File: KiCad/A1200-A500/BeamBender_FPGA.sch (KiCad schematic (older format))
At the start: 27 parts, among them J6 Conn_02x06_Odd_Even, U2 GW1NR-UV9LQ144P, U5 AK5720VT, X3 5.0x3.2mm

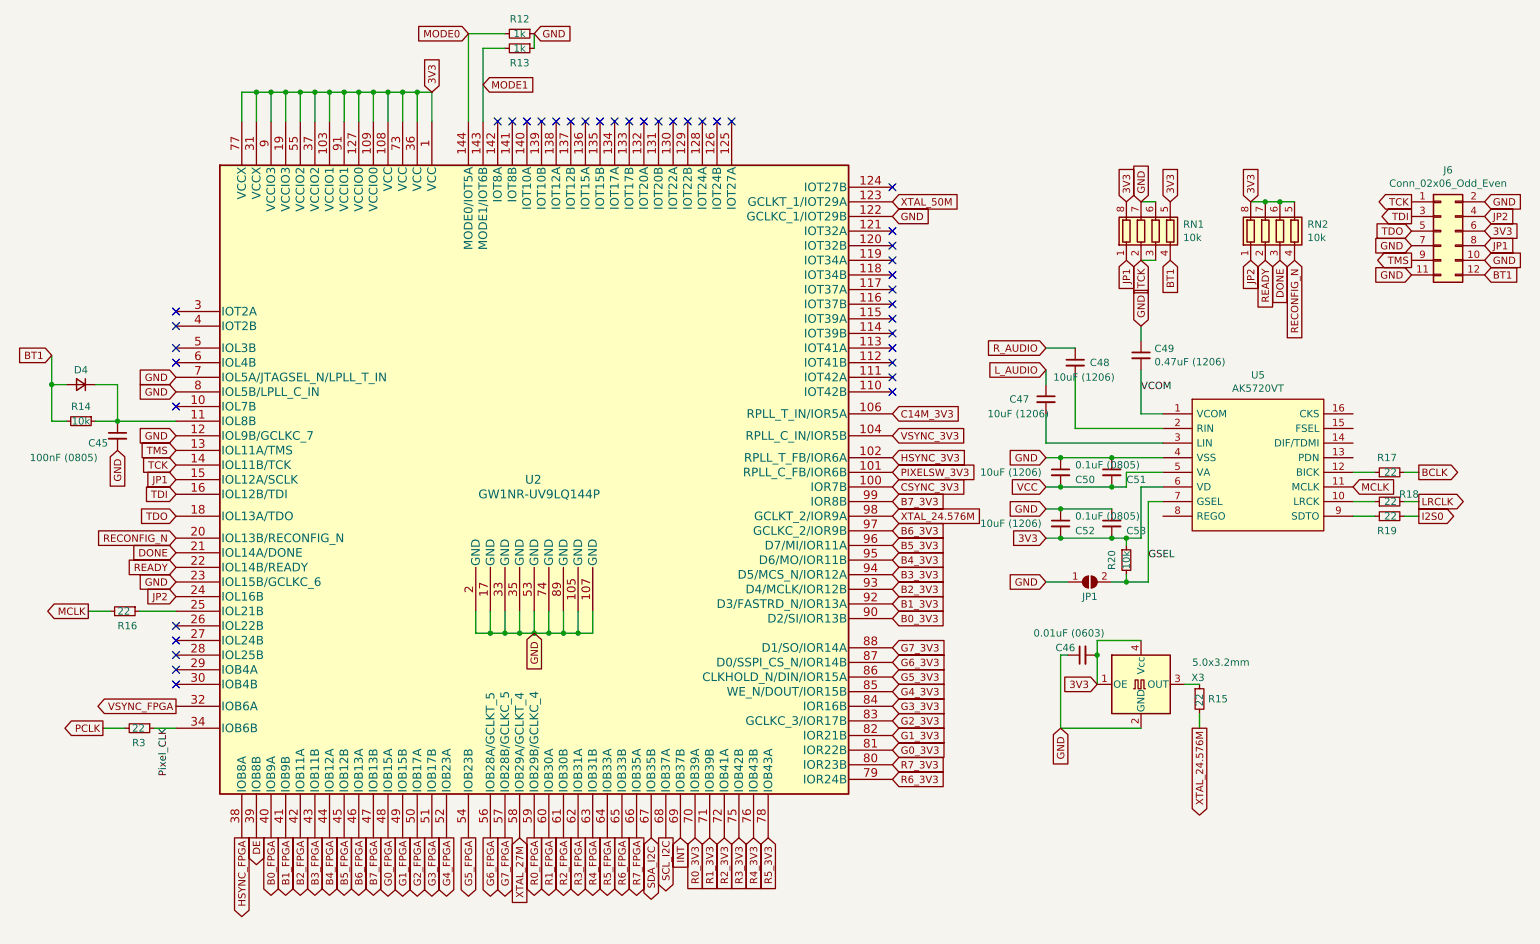
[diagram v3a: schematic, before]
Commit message: Finished routing the ak5720vt-chip, changed to a potential-divider for controlling GSEL-pin, PDN_RESET,FSEL and DIF-signals routed to spare pins in the FPGA
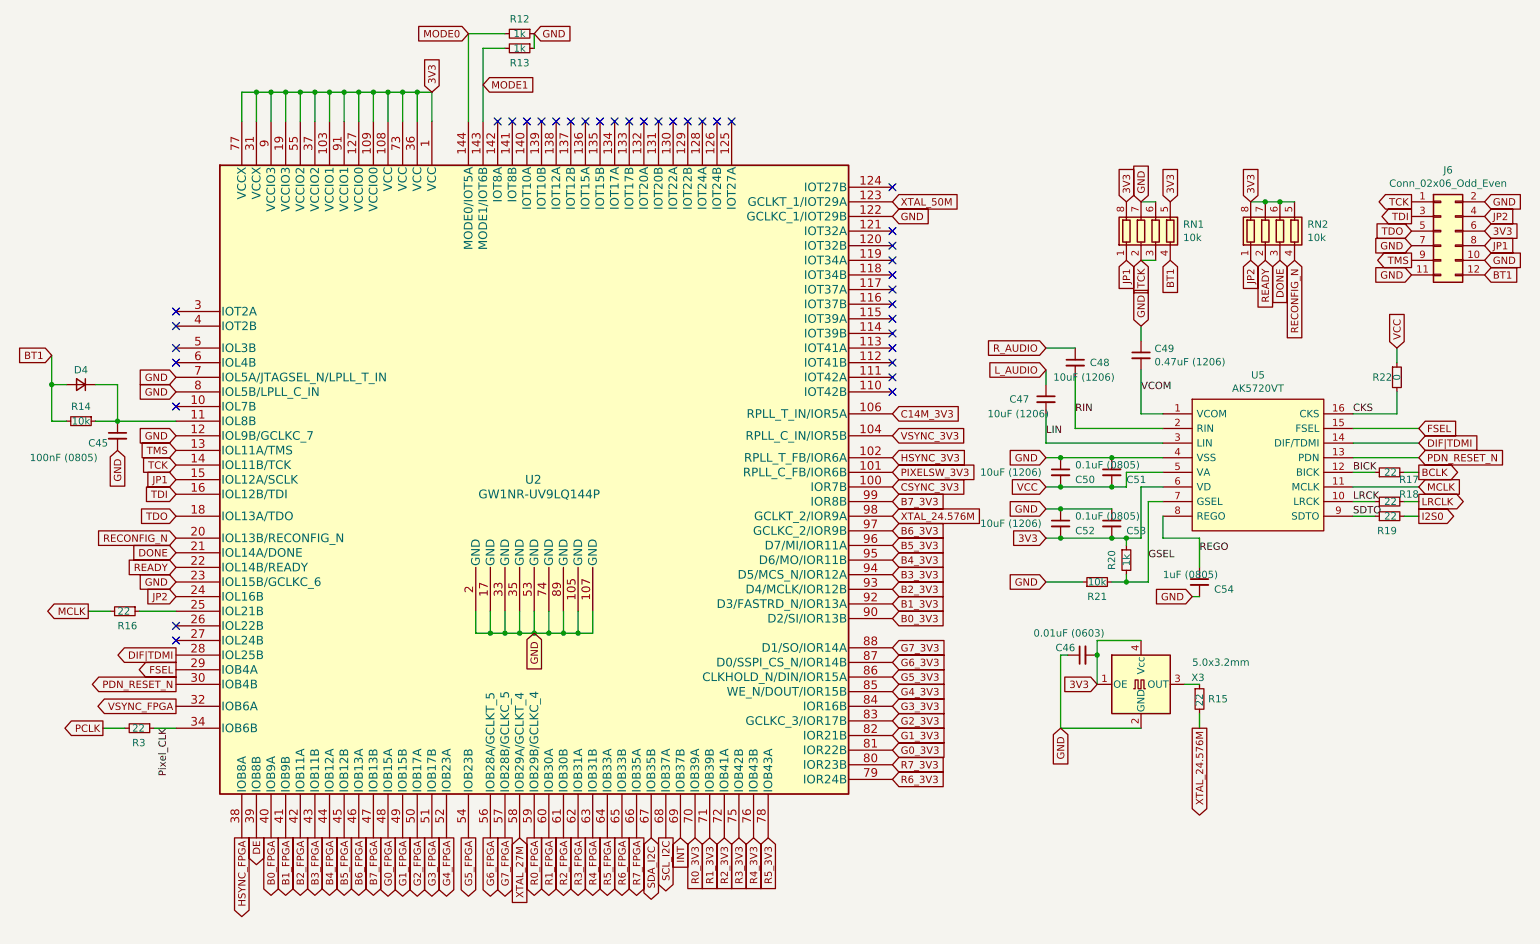
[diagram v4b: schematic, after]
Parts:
- removed JP1: SolderJumper_2_Open, Jumper:SolderJumper-2_P1.3mm_Open_Pad1.0x1.5mm, symbol Jumper:SolderJumper_2_Open
- added C54: 1uF (0805), Capacitor_SMD:C_0805_2012Metric_Pad1.18x1.45mm_HandSolder, symbol Device:C_Small
- added R21: 10k, Resistor_SMD:R_0805_2012Metric_Pad1.20x1.40mm_HandSolder, symbol Device:R_Small
- added R22: 0, Resistor_SMD:R_0805_2012Metric_Pad1.20x1.40mm_HandSolder, symbol Device:R_Small
- R20: value 10k -> 1k
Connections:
- net GND: now also C54.2, R21.1
- net GSEL: now also R21.2
- net VCC: now also R22.1
- net DIF|TDMI: now reaches U2.28 (IOL25B)
- net DIF|TDMI: now also U5.14 (DIF/TDMI)
- net FSEL: now reaches U2.29 (IOB4A)
- net FSEL: now also U5.15 (FSEL)
- net PDN_RESET_N: now reaches U2.30 (IOB4B)
- net PDN_RESET_N: now also U5.13 (PDN)
- net LRCK: now reaches R18.1, U5.10 (LRCK)
- net BICK: now reaches R17.1, U5.12 (BICK)
- net CKS: now reaches U5.16 (CKS)
- net CKS: now also R22.2
- net RIN: now reaches C48.2, U5.2 (RIN)
- net LIN: now reaches C47.2, U5.3 (LIN)
- net REGO: now reaches U5.8 (REGO)
- net REGO: now also C54.1
- net SDTO: now reaches R19.1, U5.9 (SDTO)
- no-connect marks 40 -> 37
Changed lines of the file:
@@
 NoConn ~ 1600 4700
 NoConn ~ 1600 4800
-NoConn ~ 1600 4900
-NoConn ~ 1600 5000
-NoConn ~ 1600 5100
 NoConn ~ 6500 1700
 NoConn ~ 6500 2000
@@
 Text GLabel 10100 3950 2    50   Output ~ 0
 I2S0
-Text GLabel 9650 3750 2    50   Input ~ 0
+Text GLabel 10100 3750 2    50   Input ~ 0
 MCLK
 Text GLabel 10100 3850 2    50   Output ~ 0
@@
 U 1 1 666AAB38
 P 9900 3650
-F 0 "R17" V 10000 3600 50  0000 L CNN
+F 0 "R17" V 9850 3450 50  0000 L CNN
 F 1 "22" V 9900 3600 50  0000 L CNN
 F 2 "Resistor_SMD:R_0603_1608Metric_Pad0.98x0.95mm_HandSolder" H 9900 3650 50  0001 C CNN
@@
 	8350 3850 8250 3850
 $Comp
-L Jumper:SolderJumper_2_Open JP1
-U 1 1 668D7347
-P 7850 4400
-F 0 "JP1" H 7850 4300 50  0000 C CNN
-F 1 "SolderJumper_2_Open" H 7850 4514 50  0001 C CNN
-F 2 "Jumper:SolderJumper-2_P1.3mm_Open_Pad1.0x1.5mm" H 7850 4400 50  0001 C CNN
-F 3 "~" H 7850 4400 50  0001 C CNN
-	1    7850 4400
-	1    0    0    -1
-$EndComp
-$Comp
 L Device:R_Small R20
 U 1 1 668DB86F
 P 8100 4250
 F 0 "R20" V 8000 4250 50  0000 C CNN
-F 1 "10k" V 8100 4250 50  0000 C CNN
+F 1 "1k" V 8100 4250 50  0000 C CNN
 F 2 "Resistor_SMD:R_0805_2012Metric_Pad1.20x1.40mm_HandSolder" H 8100 4250 50  0001 C CNN
 F 3 "~" H 8100 4250 50  0001 C CNN
@@
 GND
 Wire Wire Line
-	7550 4400 7700 4400
-Wire Wire Line
 	8100 4100 8100 4150
 Connection ~ 8100 4100
@@
 Text Label 8250 4250 0    50   ~ 0
 GSEL
+$Comp
+L Device:C_Small C?
+U 1 1 66921A02
+P 8600 4400
+AR Path="/66921A02" Ref="C?"  Part="1"
+AR Path="/6541C824/66921A02" Ref="C54"  Part="1"
+F 0 "C54" H 8700 4350 50  0000 L CNN
+F 1 "1uF (0805)" H 8350 4450 50  0000 L CNN
+F 2 "Capacitor_SMD:C_0805_2012Metric_Pad1.18x1.45mm_HandSolder" H 8600 4400 50  0001 C CNN
+F 3 "~" H 8600 4400 50  0001 C CNN
+	1    8600 4400
+	1    0    0    -1
+$EndComp
+Text GLabel 8550 4500 0    50   Input ~ 0
+GND
+Wire Wire Line
+	8550 4500 8600 4500
+Wire Wire Line
+	8350 3950 8350 4100
+Wire Wire Line
+	8350 4100 8600 4100
+Wire Wire Line
+	8600 4100 8600 4300
+Text Label 8600 4200 0    50   ~ 0
+REGO
+Text Label 7750 3250 0    50   ~ 0
+RIN
+Text Label 7550 3400 0    50   ~ 0
+LIN
+Text Label 9650 3650 0    50   ~ 0
+BICK
+Text Label 9650 3850 0    50   ~ 0
+LRCK
+Text Label 9650 3950 0    50   ~ 0
+SDTO
+Text Label 9650 3250 0    50   ~ 0
+CKS
+$Comp
+L Device:R_Small R22
+U 1 1 66968A2E
+P 9950 3000
+F 0 "R22" H 9850 3000 50  0000 C CNN
+F 1 "0" V 9950 3000 50  0000 C CNN
+F 2 "Resistor_SMD:R_0805_2012Metric_Pad1.20x1.40mm_HandSolder" H 9950 3000 50  0001 C CNN
+F 3 "~" H 9950 3000 50  0001 C CNN
+	1    9950 3000
+	1    0    0    -1
+$EndComp
+Wire Wire Line
+	9650 3250 9950 3250
+Wire Wire Line
+	9950 3250 9950 3100
+Text GLabel 9950 2800 1    50   Input ~ 0
+VCC
+Wire Wire Line
+	9950 2900 9950 2800
+Text GLabel 10100 3450 2    50   Input ~ 0
+DIF|TDMI
+Wire Wire Line
+	9650 3450 10100 3450
+Text GLabel 10100 3550 2    50   Input ~ 0
+PDN_RESET_N
+Wire Wire Line
+	10100 3550 9650 3550
+Wire Wire Line
+	9650 3750 10100 3750
+Text GLabel 1600 5100 0    50   Output ~ 0
+PDN_RESET_N
+Text GLabel 1600 4900 0    50   Output ~ 0
+DIF|TDMI
+Text GLabel 10100 3350 2    50   Input ~ 0
+FSEL
+Wire Wire Line
+	9650 3350 10100 3350
+Text GLabel 1600 5000 0    50   Output ~ 0
+FSEL
+$Comp
+L Device:R_Small R21
+U 1 1 66A36561
+P 7900 4400
+F 0 "R21" V 7800 4400 50  0000 C CNN
+F 1 "10k" V 7900 4400 50  0000 C CNN
+F 2 "Resistor_SMD:R_0805_2012Metric_Pad1.20x1.40mm_HandSolder" H 7900 4400 50  0001 C CNN
+F 3 "~" H 7900 4400 50  0001 C CNN
+	1    7900 4400
+	0    -1   -1   0
+$EndComp
+Wire Wire Line
+	7550 4400 7800 4400
 $EndSCHEMATC

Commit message: Fixed assignment/enumeration of all capacitors from C1 to C54
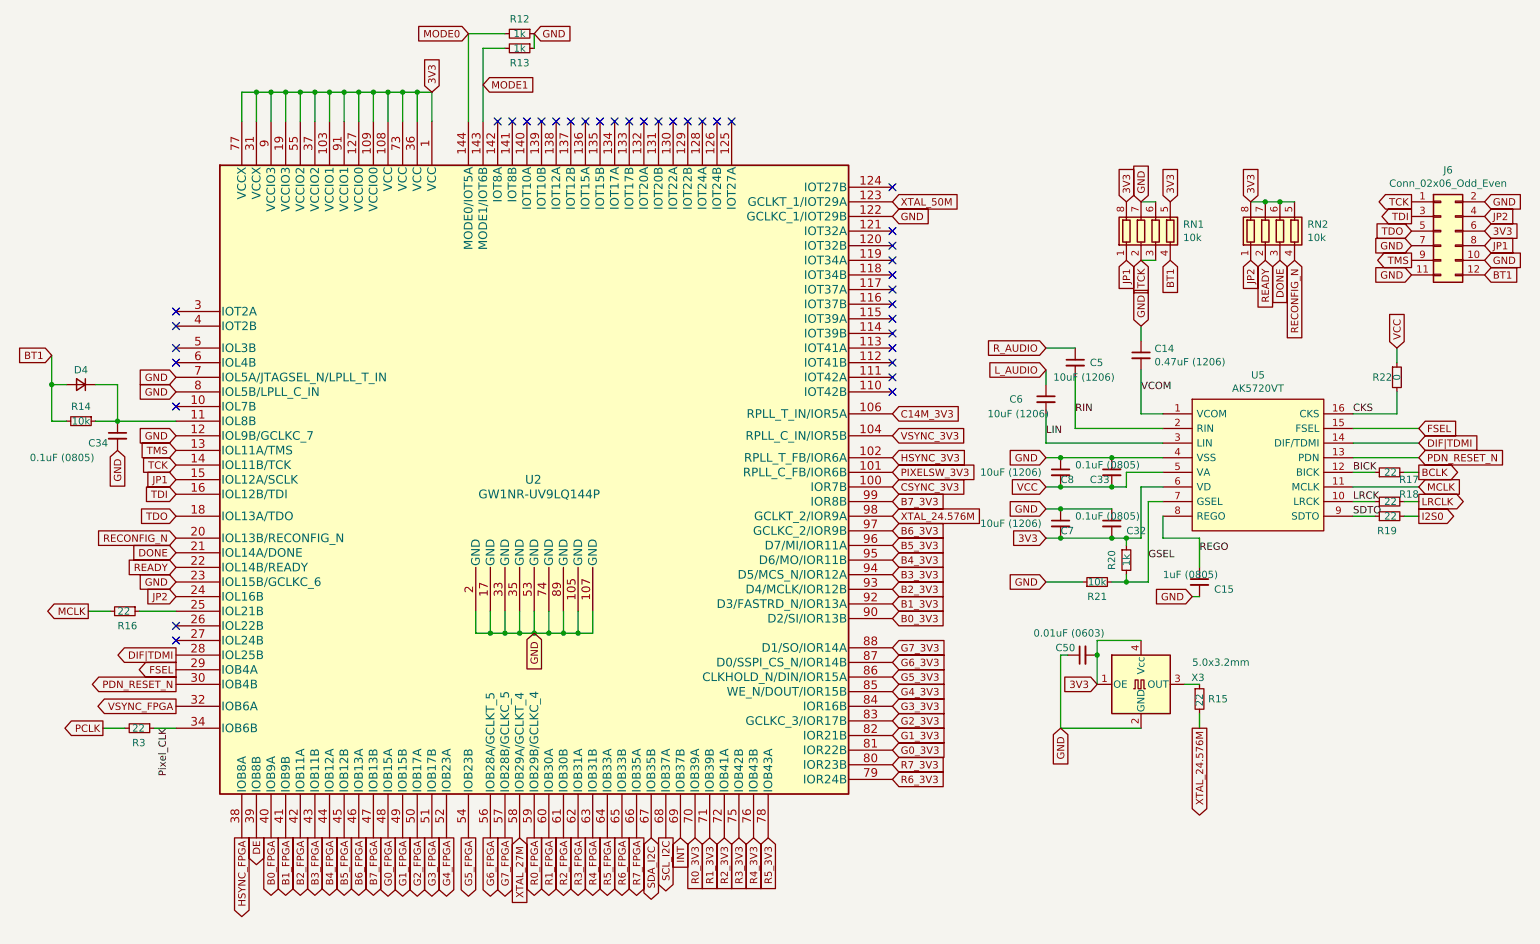
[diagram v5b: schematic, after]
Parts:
- C34: renamed from C45; value 100nF (0805) -> 0.1uF (0805)
- renumbered C49 to C14, C54 to C15, C53 to C32, C51 to C33, C48 to C5, C46 to C50, C47 to C6, C52 to C7, C50 to C8
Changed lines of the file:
@@
 $EndComp
 $Comp
-L Device:C_Small C45
+L Device:C_Small C34
 U 1 1 66517D93
 P 1200 3400
-F 0 "C45" H 1000 3350 50  0000 L CNN
-F 1 "100nF (0805)" H 600 3250 50  0000 L CNN
+F 0 "C34" H 1000 3350 50  0000 L CNN
+F 1 "0.1uF (0805)" H 600 3250 50  0000 L CNN
 F 2 "Capacitor_SMD:C_0805_2012Metric_Pad1.18x1.45mm_HandSolder" H 1200 3400 50  0001 C CNN
 F 3 "~" H 1200 3400 50  0001 C CNN
@@
 XTAL_24.576M
 $Comp
-L Device:C_Small C46
+L Device:C_Small C50
 U 1 1 665DD14C
 P 7800 4900
-F 0 "C46" V 7850 4950 50  0000 L CNN
+F 0 "C50" V 7850 4950 50  0000 L CNN
 F 1 "0.01uF (0603)" V 7950 4750 50  0000 L CNN
 F 2 "Capacitor_SMD:C_0603_1608Metric_Pad1.08x0.95mm_HandSolder" H 7800 4900 50  0001 C CNN
@@
 R_AUDIO
 $Comp
-L Device:C_Small C48
+L Device:C_Small C5
 U 1 1 667B6179
 P 7750 2900
-F 0 "C48" H 7850 2900 50  0000 L CNN
+F 0 "C5" H 7850 2900 50  0000 L CNN
 F 1 "10uF (1206)" H 7600 2800 50  0000 L CNN
 F 2 "Capacitor_SMD:C_1206_3216Metric_Pad1.33x1.80mm_HandSolder" H 7750 2900 50  0001 C CNN
@@
 $EndComp
 $Comp
-L Device:C_Small C47
+L Device:C_Small C6
 U 1 1 667B7F1E
 P 7550 3150
-F 0 "C47" H 7300 3150 50  0000 L CNN
+F 0 "C6" H 7300 3150 50  0000 L CNN
 F 1 "10uF (1206)" H 7150 3050 50  0000 L CNN
 F 2 "Capacitor_SMD:C_1206_3216Metric_Pad1.33x1.80mm_HandSolder" H 7550 3150 50  0001 C CNN
@@
 	7550 2950 7550 3050
 $Comp
-L Device:C_Small C49
+L Device:C_Small C14
 U 1 1 667DACF3
 P 8200 2850
-F 0 "C49" H 8292 2896 50  0000 L CNN
+F 0 "C14" H 8292 2896 50  0000 L CNN
 F 1 "0.47uF (1206)" H 8292 2805 50  0000 L CNN
 F 2 "Capacitor_SMD:C_1206_3216Metric_Pad1.33x1.80mm_HandSolder" H 8200 2850 50  0001 C CNN
@@
 	7650 3550 8000 3550
 $Comp
-L Device:C_Small C50
+L Device:C_Small C8
 U 1 1 66802342
 P 7650 3650
-F 0 "C50" H 7750 3600 50  0000 L CNN
+F 0 "C8" H 7650 3600 50  0000 L CNN
 F 1 "10uF (1206)" H 7100 3650 50  0000 L CNN
 F 2 "Capacitor_SMD:C_1206_3216Metric_Pad1.33x1.80mm_HandSolder" H 7650 3650 50  0001 C CNN
@@
 P 8000 3650
 AR Path="/66811715" Ref="C?"  Part="1"
-AR Path="/6541C824/66811715" Ref="C51"  Part="1"
-F 0 "C51" H 8100 3600 50  0000 L CNN
+AR Path="/6541C824/66811715" Ref="C33"  Part="1"
+F 0 "C33" H 7850 3600 50  0000 L CNN
 F 1 "0.1uF (0805)" H 7750 3700 50  0000 L CNN
 F 2 "Capacitor_SMD:C_0805_2012Metric_Pad1.18x1.45mm_HandSolder" H 8000 3650 50  0001 C CNN
@@
 	7650 3900 8000 3900
 $Comp
-L Device:C_Small C52
+L Device:C_Small C7
 U 1 1 668486F6
 P 7650 4000
-F 0 "C52" H 7750 3950 50  0000 L CNN
+F 0 "C7" H 7650 3950 50  0000 L CNN
 F 1 "10uF (1206)" H 7100 4000 50  0000 L CNN
 F 2 "Capacitor_SMD:C_1206_3216Metric_Pad1.33x1.80mm_HandSolder" H 7650 4000 50  0001 C CNN
@@
 P 8000 4000
 AR Path="/66848700" Ref="C?"  Part="1"
-AR Path="/6541C824/66848700" Ref="C53"  Part="1"
-F 0 "C53" H 8100 3950 50  0000 L CNN
+AR Path="/6541C824/66848700" Ref="C32"  Part="1"
+F 0 "C32" H 8100 3950 50  0000 L CNN
 F 1 "0.1uF (0805)" H 7750 4050 50  0000 L CNN
 F 2 "Capacitor_SMD:C_0805_2012Metric_Pad1.18x1.45mm_HandSolder" H 8000 4000 50  0001 C CNN
@@
 P 8600 4400
 AR Path="/66921A02" Ref="C?"  Part="1"
-AR Path="/6541C824/66921A02" Ref="C54"  Part="1"
-F 0 "C54" H 8700 4350 50  0000 L CNN
+AR Path="/6541C824/66921A02" Ref="C15"  Part="1"
+F 0 "C15" H 8700 4350 50  0000 L CNN
 F 1 "1uF (0805)" H 8350 4450 50  0000 L CNN
 F 2 "Capacitor_SMD:C_0805_2012Metric_Pad1.18x1.45mm_HandSolder" H 8600 4400 50  0001 C CNN
